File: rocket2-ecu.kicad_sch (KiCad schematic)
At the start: 25 parts, among them J1 ALARM, J2 SMA, P1 PAD_SMD, P2 PAD_SMD, P3 PAD_SMD, P4 PAD_SMD, Q1 DMG3402L

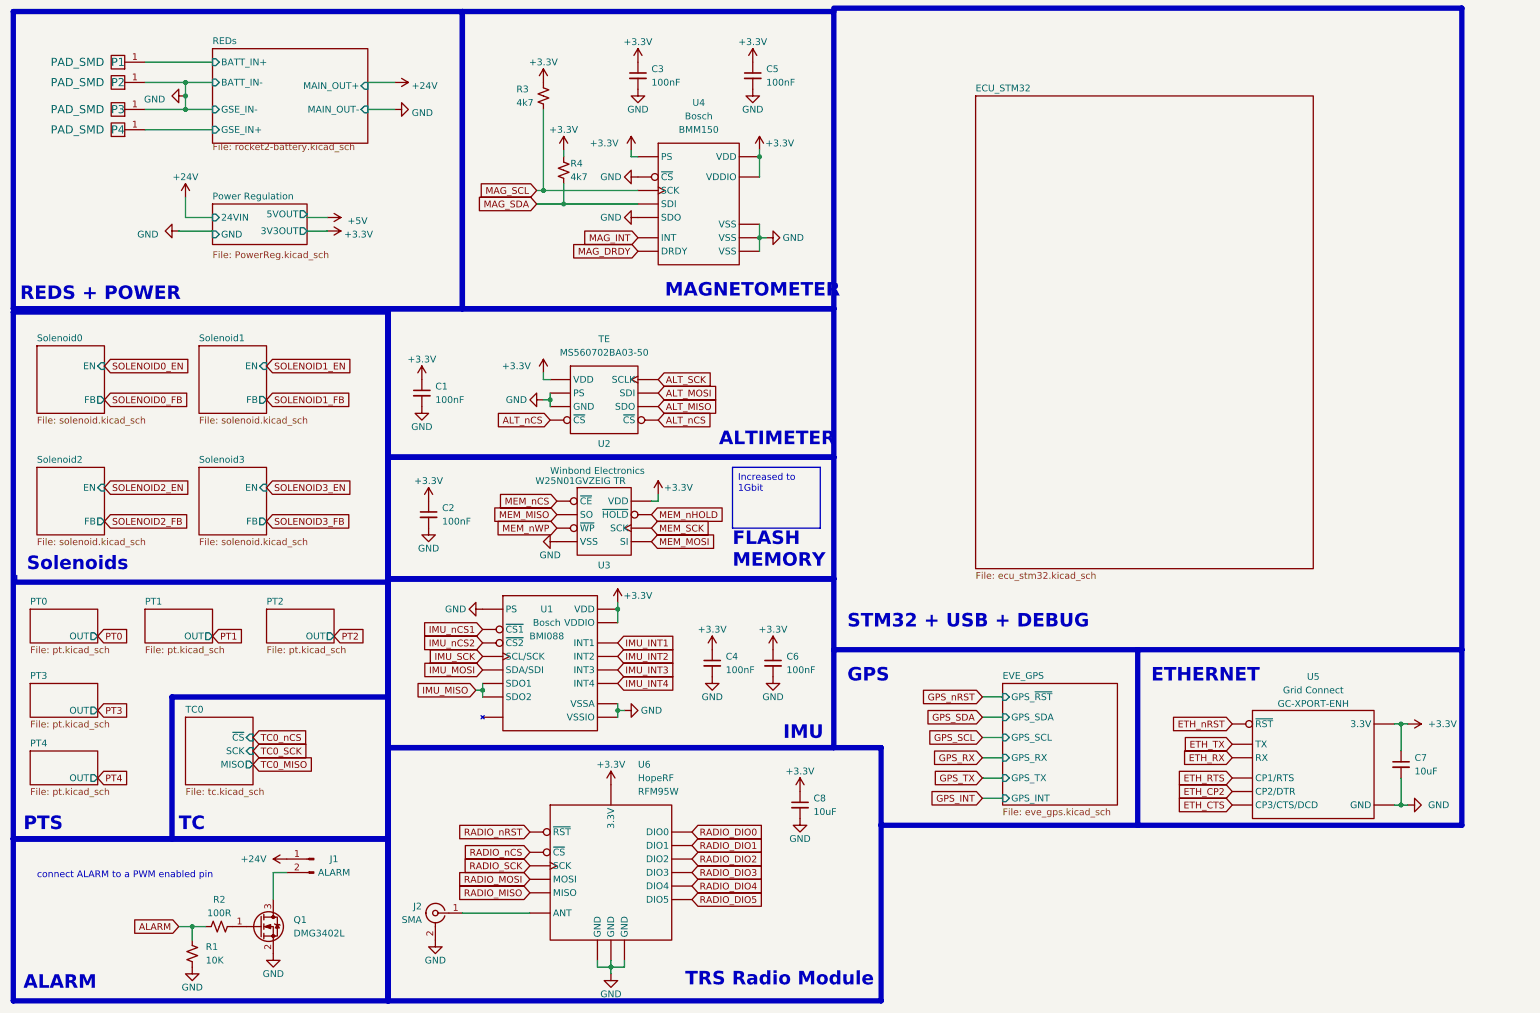
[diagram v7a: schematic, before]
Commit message: 8.02 Update; Also changed VRMs and added some notes
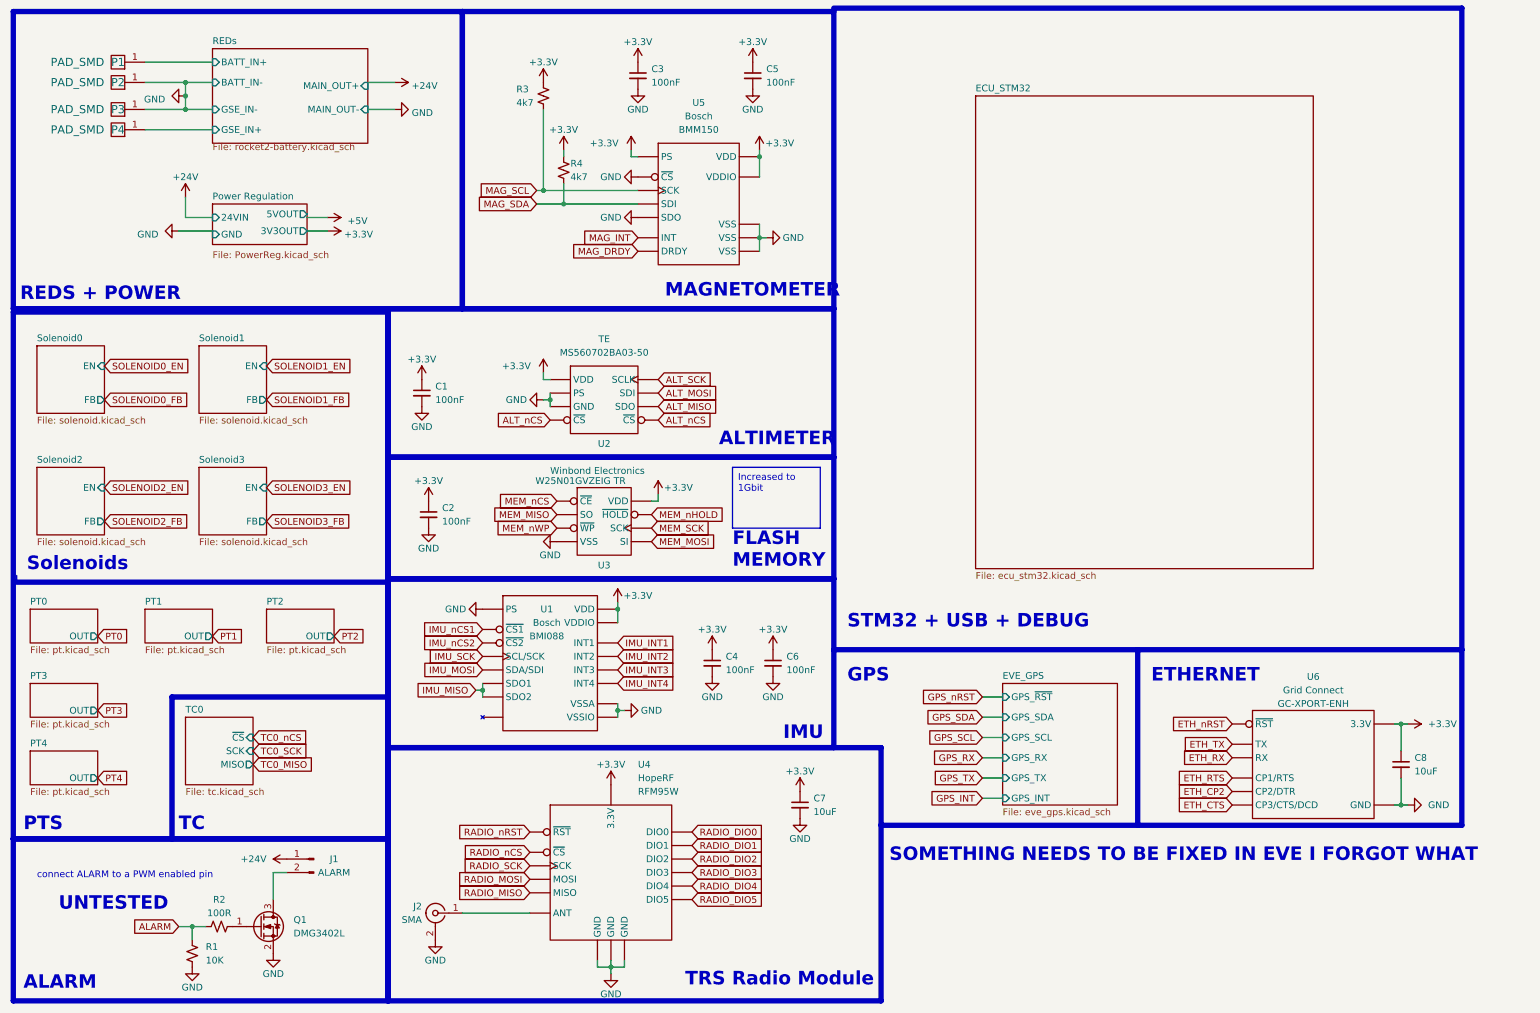
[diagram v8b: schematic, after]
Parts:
- renumbered C8 to C7, C7 to C8, U6 to U4, U4 to U5, U5 to U6
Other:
- note added: "SOMETHING NEEDS TO BE FIXED IN EVE I FORGOT WHAT"
- note added: "UNTESTED"
